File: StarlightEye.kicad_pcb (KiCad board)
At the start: 4 copper layers, 44.3 x 39 mm, 96 parts, among them J1 QWIIC_CONNECTORJS-1MM, J2 FH12A-22S-0.5SH(55), J3 Conn_Coaxial, J4 Conn_Coaxial, J5 Conn_Coaxial, Q1 DMG2302UK-7, Q2 DMG2302UK-7, U1 AP3418KTR-G1, U2 LP5907MFX-1.8, U3 AP2161W, U4 IMX585, U5 ECS-2520MV-240-DN-TR

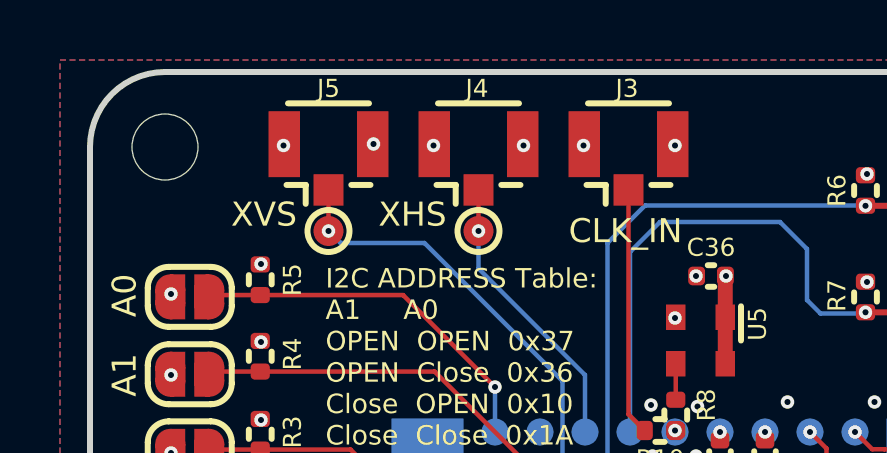
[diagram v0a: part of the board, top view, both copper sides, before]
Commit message: Bug fix: swaping part no AP2161W with AP2171W to have the correct EN polarity
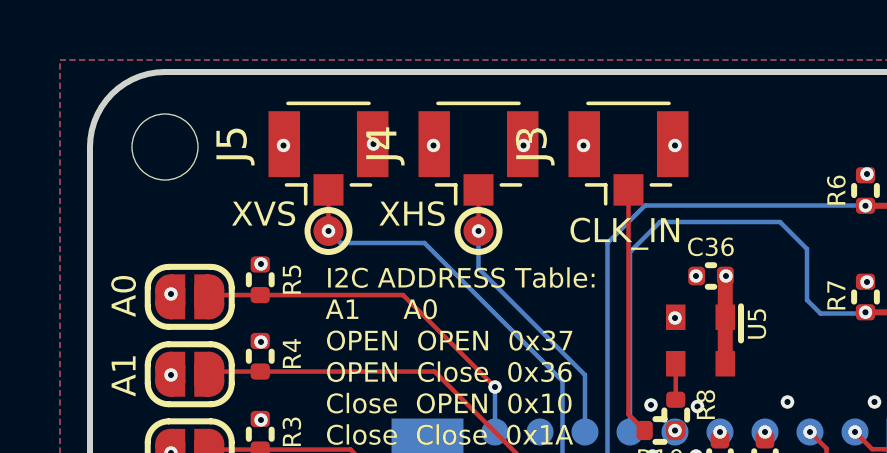
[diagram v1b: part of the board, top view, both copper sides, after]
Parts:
- R1: value 10K -> 13.7K
- R2: value 10K -> 16.5K
- U3: value AP2161W -> AP2171W

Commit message: V1.6 init
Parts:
- removed FB1, FB2: BLM18KG102SN1D, Inductor_SMD:L_0603_1608Metric
- removed Q1, Q2: DMG2302UK-7, Package_TO_SOT_SMD:SOT-23
- removed TP5: TestPoint, TestPoint:TestPoint_Pad_D1.0mm
- added C48: 100nF, Capacitor_SMD:C_0402_1005Metric, F.Cu at (141.1, 110.5)
- added C49: 10nF, Capacitor_SMD:C_0402_1005Metric, F.Cu at (129.4, 111.0)
- added C50: 10uF, Capacitor_SMD:C_0603_1608Metric, F.Cu at (132.7, 107.5)
- added C51: 100nF, Capacitor_SMD:C_0402_1005Metric, F.Cu at (156.6, 120.9)
- added C52: 100nF, Capacitor_SMD:C_0402_1005Metric, F.Cu at (156.6, 119.0)
- added C53: 100nF, Capacitor_SMD:C_0402_1005Metric, F.Cu at (151.6, 117.4)
- added C54: 100nF, Capacitor_SMD:C_0402_1005Metric, F.Cu at (151.7, 120.8)
- added C55: 100nF, Capacitor_SMD:C_0402_1005Metric, F.Cu at (153.4, 89.0)
- added C56: 100nF, Capacitor_SMD:C_0402_1005Metric, F.Cu at (154.2, 94.8)
- added C57: 10nF, Capacitor_SMD:C_0402_1005Metric, F.Cu at (132.3, 105.0)
- added C58: 100pF, Capacitor_SMD:C_0402_1005Metric, F.Cu at (139.2, 117.0)
- added C59: 4.7uF, Capacitor_SMD:C_0603_1608Metric, F.Cu at (126.1, 117.4)
- added C60: C_Feedthrough, footprints:NFM18CC101R1C3D, F.Cu at (155.9, 115.1)
- added C61: 120pF, Capacitor_SMD:C_0402_1005Metric, F.Cu at (129.4, 113.0)
- added C62: 22uF, Capacitor_SMD:C_0805_2012Metric, F.Cu at (128.4, 114.9)
- added D1: MBR0540, Diode_SMD:D_SOD-123, F.Cu at (159.7, 113.9)
- added FB4: BLM18KG102SN1D, Inductor_SMD:L_0402_1005Metric, F.Cu at (141.1, 113.5)
- added J6: Conn_01x02_Shielded, Connector_Molex:Molex_PicoBlade_53398-0271_1x02-1MP_P1.25mm_Vertical, B.Cu at (164.9, 117.3)
- added J7: Conn_01x02_Shielded, Connector_Molex:Molex_PicoBlade_53261-0271_1x02-1MP_P1.25mm_Horizontal, F.Cu at (164.4, 117.7)
- added R11: 10K, Resistor_SMD:R_0402_1005Metric, F.Cu at (155.4, 122.3)
- added R12: 1.15K, Resistor_SMD:R_0402_1005Metric, F.Cu at (130.3, 105.0)
- added R13: 10K, Resistor_SMD:R_0402_1005Metric, F.Cu at (128.4, 113.0)
- added R14: 2K, Resistor_SMD:R_0402_1005Metric, F.Cu at (127.4, 113.0)
- added TP14: TestPoint, TestPoint:TestPoint_Pad_D1.0mm, F.Cu at (131.2, 121.8)
- added TP7: TestPoint, TestPoint:TestPoint_Pad_D1.0mm, F.Cu at (141.4, 121.3)
- added TP_3V1: TestPoint, TestPoint:TestPoint_Pad_D1.0mm, F.Cu at (125.9, 112.8)
- added U10: TVS0500DRV, Package_SON:WSON-6-1EP_2x2mm_P0.65mm_EP1x1.6mm, F.Cu at (158.6, 116.5)
- added U11: TPSM82821SILR, footprints:TPSM82821SILR, F.Cu at (128.4, 117.4)
- added U6: TMP117AIDRVR, footprints:TMP117AIDRVR, F.Cu at (142.9, 110.8)
- added U7: STM8S003F3P, Package_SO:TSSOP-20_4.4x6.5mm_P0.65mm, F.Cu at (146.6, 119.7)
- added U8: DRV8837C, Package_SON:WSON-8-1EP_2x2mm_P0.5mm_EP0.9x1.6mm, F.Cu at (154.7, 119.7)
- added U9: TCA9406DC, footprints:TCA9406DCUR, F.Cu at (153.4, 92.0)
- C13: value 4.7uF -> C_Feedthrough; footprint Capacitor_SMD:C_0603_1608Metric -> footprints:NFM18CC101R1C3D
- C32: value 4.7uF -> 10uF
- J1: value QWIIC_CONNECTORJS-1MM -> Conn_01x04_Shielded
- R6: value 1K -> 10K
- R7: value 1K -> 3.57K
- U3: value AP2171W -> TPS7A90; footprint Package_TO_SOT_SMD:SOT-23-5 -> Package_DFN_QFN:Texas_S-PDSO-N10_EP1.2x2mm
- moved R7 56.5 mm to (131.3, 105.0), turned to 90 degrees
- moved R6 51.2 mm to (147.7, 113.4)
- moved TP1 39.7 mm to (139.1, 113.5)
- moved C22 38.2 mm to (136.1, 115.0)
- moved C24 38.2 mm to (136.1, 120.8)
- moved L1 38.2 mm to (133.6, 116.1)
- moved U1 38.2 mm to (136.3, 118.0)
- moved R1 38.1 mm to (139.2, 118.0)
- moved R2 38.1 mm to (139.2, 119.1)
- moved C32 36.4 mm to (132.0, 111.0), turned to 0 degrees
- moved FB3 36.3 mm to (136.2, 122.5), turned to 0 degrees
- moved C13 35.3 mm to (131.1, 113.1), turned to 90 degrees
- moved U3 34.8 mm to (130.3, 108.1)
- moved C41 34.6 mm to (135.1, 109.4)
- moved TP10 34.5 mm to (137.3, 98.7)
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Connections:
- C13 pad 1: GND -> Net-(C12-Pad2)
- C13 pad 2: Net-(C13-Pad2) -> GND
- C32 pad 1: +3.3VA -> Net-(U3-Pad10)
- FB3 pad 2: +3V3 -> +5V
- J1 pad MP: (no net) -> GND
- J2 pad MP: (no net) -> GND
- JP1 pad 1: GND -> +1V8
- JP2 pad 1: GND -> +1V8
- R4 pad 2: +1V8 -> GND
- R5 pad 1: +1V8 -> ADDR0
- R5 pad 2: ADDR0 -> GND
- R6 pad 1: SCL_1V8 -> CAM_EN
- R6 pad 2: +1V8 -> GND
- R7 pad 1: +1V8 -> Net-(U3-Pad3)
- R7 pad 2: SDA_1V8 -> +3.3VA
- U3 pad 2: GND -> +3.3VA
- U3 pad 3: unconnected-(U3-Pad3) -> Net-(U3-Pad3)
- U3 pad 4: CAM_EN -> GND
- U3 pad 5: Net-(C13-Pad2) -> unconnected-(U3-Pad5)
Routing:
- net +3V3: track 70.9 -> 13.6 mm, vias 2 -> 11
- net SDA_3V3: track 37.7 -> 63.2 mm, vias 2 -> 0
- net SCL_3V3: track 39.3 -> 62.6 mm, vias 0 -> 4
- net +1V8: track 28.2 -> 41.4 mm, vias 21 -> 14
- net Net-(J6-Pad1): track 0.00 -> 10.7 mm, vias 0 -> 1
- net Net-(J6-Pad2): track 0.00 -> 9.68 mm, vias 0 -> 1
- net SLEEP: track 0.00 -> 7.30 mm
- net Net-(J3-Pad1): track 8.24 -> 1.31 mm
- net IN1: track 0.00 -> 6.00 mm
- net Net-(D1-Pad2): track 0.00 -> 6.00 mm
- net CLOCK: track 0.00 -> 5.55 mm
- net Net-(C61-Pad2): track 0.00 -> 5.35 mm
- net IN2: track 0.00 -> 5.05 mm
- net +1V1: track 19.8 -> 15.5 mm, vias 18 -> 19
- net CAM_EN: track 51.0 -> 47.0 mm
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- added copper zone on In2.Cu, net +3V3
- added copper zone on B.Cu, net +5V
- added copper zone on F.Cu, net +5V
- added copper zone on In2.Cu, net +5V
- added copper zone on F.Cu, net Net-(C12-Pad2)
- added copper zone on In2.Cu, net Net-(C12-Pad2)
- added copper zone on F.Cu, net Net-(C60-Pad1)
- added copper zone on F.Cu, net Net-(U3-Pad10)
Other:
- outline, holes or cut-outs redrawn
- board text added: "*"
- board text added: "+"
- board text added: "-"
- board text added: "3V3 FPC"
- board text added: "5V"
- board text added: "5V IN"
- board text added: "AD0"
- board text added: "AD1"
- board text added: "CLK"
- board text added: "Close: MASTER"
- board text added: "FPC Contact Pin Facing UP"
- board text added: "I2C ADDRESS Table: AD1 AD0 OPEN OPEN 0x1A <-Default OPEN Close 0x10 Close OPEN 0x36 Close Close 0x37"
- board text added: "IR Switch"
- board text added: "SWIO"
- board text added: "StarlightEye v1.6 Designed by Will Whang 2024/02/03"
- board text added: "Use FPC with contact pin on the same side"
- board text added: "VINT"
- board text removed: "3V3"
- board text removed: "A0"
- board text removed: "A1"
- board text removed: "CLK_IN"
- board text removed: "Close:MASTER"
- board text removed: "FPC Contact Facing UP"
- board text removed: "I2C ADDRESS Table: A1 A0 OPEN OPEN 0x37 OPEN Close 0x36 Close OPEN 0x10 Close Close 0x1A"
- board text removed: "StarlightEye v1.0 Designed by Will Whang 2023/04/07"

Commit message: V1.7
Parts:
- added C63: 100n, Capacitor_SMD:C_0402_1005Metric, F.Cu at (153.3, 92.6)
- added C64: 10nF, Capacitor_SMD:C_0402_1005Metric, F.Cu at (151.4, 92.6)
- added C65: 2.2uF, Capacitor_SMD:C_0402_1005Metric, F.Cu at (153.3, 93.6)
- added U12: ICM-42688-P, footprints:PQFN50P300X250X97-14N, F.Cu at (152.6, 90.5)
- moved TP4 26.2 mm to (152.6, 115.2)
- moved TP6 3.60 mm to (149.1, 87.0)
- moved U9 3.20 mm to (156.7, 92.0)
- moved C55 3.20 mm to (156.6, 89.0)
- moved C56 3.20 mm to (157.4, 94.8)
- moved C36 1.48 mm to (146.9, 90.2)
- moved U5 1.34 mm to (146.5, 92.2)
- moved R10 1.25 mm to (143.6, 92.5)
- moved R8 1.25 mm to (144.1, 93.0)
- moved TP13 0.35 mm to (130.8, 100.0)
- moved U6 0.25 mm to (142.9, 111.0)
- moved C41 0.20 mm to (135.3, 109.4)
- turned R3 to -90 degrees
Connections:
- JP3 pad 1: GND -> +1V8
- R3 pad 1: XMASTER -> GND
- R3 pad 2: +1V8 -> XMASTER
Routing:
- net XVS: track 14.5 -> 34.2 mm, vias 1 -> 4
- net SCL_1V8: track 15.9 -> 26.5 mm
- net SDA_1V8: track 14.6 -> 25.0 mm
- net +1V8: track 41.4 -> 49.0 mm, vias 14 -> 18
- net GND: track 0.00 -> 6.48 mm, vias 232 -> 253
- net SCL_3V3: track 62.6 -> 59.1 mm
- net SDA_3V3: track 63.2 -> 60.0 mm
- net Net-(J3-Pad1): track 1.31 -> 2.56 mm
- net CLOCK: track 5.55 -> 4.35 mm
- net +3.3VA: track 9.15 -> 8.43 mm
- net Net-(R8-Pad2): track 1.60 -> 1.08 mm
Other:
- board text added: "0x34"
- board text added: "0x48"
- board text added: "0x68"
- board text added: "FPC Contact Facing UP"
- board text added: "JP3"
- board text added: "StarlightEye v1.7 Designed by Will Whang 2024/08/03"
- board text added: "X"
- board text added: "Y"
- board text added: "Z"
- board text removed: "Close: MASTER"
- board text removed: "FPC Contact Pin Facing UP"
- board text removed: "StarlightEye v1.6 Designed by Will Whang 2024/02/03"

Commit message: Ver 2.0 HW
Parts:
- removed D1: MBR0540, Diode_SMD:D_SOD-123
- removed J7: Conn_01x02_Shielded, Connector_Molex:Molex_PicoBlade_53261-0271_1x02-1MP_P1.25mm_Horizontal
- removed TP11, TP12, TP14, TP6: TestPoint, TestPoint:TestPoint_Pad_D1.0mm
- removed U12: ICM-42688-P, footprints:PQFN50P300X250X97-14N
- added C66: 10nF, Capacitor_SMD:C_0402_1005Metric, F.Cu at (111.4, 56.9)
- added C67: 1uF, Capacitor_SMD:C_0402_1005Metric, F.Cu at (113.3, 57.9)
- added R21: DNP, Resistor_SMD:R_0402_1005Metric, F.Cu at (106.7, 53.2)
- added R22: DNP, Resistor_SMD:R_0402_1005Metric, F.Cu at (108.1, 53.2)
- added TP5: TestPoint, TestPoint:TestPoint_Pad_D1.0mm, F.Cu at (99.7, 53.4)
- C13: value C_Feedthrough -> NFM18PC104R1C3D
- C48: value 100nF -> 1uF
- C49: value 10nF -> 1uF
- C50: value 10uF -> 22uF
- C59: value 4.7uF -> 22uF
- C60: value C_Feedthrough -> 47uF; footprint footprints:NFM18CC101R1C3D -> Capacitor_SMD:C_0603_1608Metric
- C61: value 120pF -> 100pF
- C62: value 22uF -> 47uF; footprint Capacitor_SMD:C_0805_2012Metric -> Capacitor_SMD:C_0603_1608Metric
- C63: value 100n -> 22uF; footprint Capacitor_SMD:C_0402_1005Metric -> Capacitor_SMD:C_0603_1608Metric
- C64: value 10nF -> 10uF; footprint Capacitor_SMD:C_0402_1005Metric -> Capacitor_SMD:C_0603_1608Metric
- C65: value 2.2uF -> 100nF
- FL1, FL2, FL3, FL4, FL5: value DLP11SN900HL2L -> DLM0QSB120HY2D; footprint footprints:DLP11SA350HL2B -> footprints:DLM0QSB120HY2D
- J1: footprint Connector_JST:JST_SH_SM04B-SRSS-TB_1x04-1MP_P1.00mm_Horizontal -> Connector_JST:JST_SH_BM04B-SRSS-TB_1x04-1MP_P1.00mm_Vertical
- J2: value FH12A-22S-0.5SH(55) -> TF38-22S-0.5SV(830); footprint Connector_FFC-FPC:Hirose_FH12-22S-0.5SH_1x22-1MP_P0.50mm_Horizontal -> footprints:TF3822S05SV830
- J6: footprint Connector_Molex:Molex_PicoBlade_53398-0271_1x02-1MP_P1.25mm_Vertical -> Connector_Molex:Molex_PicoBlade_53261-0271_1x02-1MP_P1.25mm_Horizontal; moved to F.Cu
- R10: value 22R -> DNP
- R13: value 10K -> 562K
- R14: value 2K -> 91K
- U10: value TVS0500DRV -> TPSM83100SIUR; footprint Package_SON:WSON-6-1EP_2x2mm_P0.65mm_EP1x1.6mm -> footprints:MICROSIP8_SIU_TEX-L
- U11: value TPSM82821SILR -> ICM-42688-P; footprint footprints:TPSM82821SILR -> footprints:PQFN50P300X250X97-14N
- U5: value ECS-2520MV-240-DN-TR -> SX2M24.000M20F30TNN
- U7: value STM8S003F3P -> CH32V003F4P6
- moved U10 77.4 mm to (88.4, 83.8), turned to -90 degrees
- moved C60 77.4 mm to (86.8, 80.2), turned to 0 degrees
- moved TP9 65.0 mm to (90.1, 87.1)
- moved C63 64.6 mm to (89.9, 80.2), turned to 0 degrees
- moved U11 64.5 mm to (112.4, 54.9), turned to 0 degrees
- moved R6 64.1 mm to (90.5, 84.5)
- moved R11 62.7 mm to (108.1, 81.3)
- moved C51 61.0 mm to (110.8, 80.5), turned to -90 degrees
- moved C54 61.0 mm to (105.1, 81.3), turned to 180 degrees
- moved J6 60.8 mm to (112.7, 86.1), turned to 0 degrees
- moved C53 60.5 mm to (103.1, 81.3)
- moved C52 59.2 mm to (110.3, 82.0), turned to 0 degrees
- moved U8 57.1 mm to (112.7, 81.0), turned to 90 degrees
- moved FB3 55.0 mm to (93.8, 87.4)
- moved C56 54.6 mm to (116.4, 58.8)
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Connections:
- net Net-(FL1-Pad2) renamed /D0_N
- net Net-(FL1-Pad3) renamed /D0_P
- net Net-(FL2-Pad2) renamed /D1_N
- net Net-(FL2-Pad3) renamed /D1_P
- net Net-(FL3-Pad2) renamed /CLK_N
- net Net-(FL3-Pad3) renamed /CLK_P
- net Net-(FL4-Pad2) renamed /D2_N
- net Net-(FL4-Pad3) renamed /D2_P
- net Net-(FL5-Pad2) renamed /D3_N
- net Net-(FL5-Pad3) renamed /D3_P
- C12 pad 2: Net-(C12-Pad2) -> +3.6V
- C13 pad 1: Net-(C12-Pad2) -> +3.6V
- C24 pad 1: Net-(C24-Pad1) -> Net-(U1-VIN)
- C52 pad 2: +5V -> +3.6V
- C59 pad 2: +5V -> +3V3
- C60 pad 1: Net-(C60-Pad1) -> +3.6V
- C61 pad 1: Net-(C12-Pad2) -> +3.6V
- C61 pad 2: Net-(C61-Pad2) -> Net-(U10-FB)
- C62 pad 1: Net-(C12-Pad2) -> +3.6V
- C63 pad 1: +1V8 -> GND
- C63 pad 2: GND -> +3V3
- C64 pad 1: +1V8 -> GND
- C64 pad 2: GND -> +3.6V
- FB3 pad 1: Net-(C24-Pad1) -> +3V3
- FB3 pad 2: +5V -> Net-(U1-VIN)
- J3 pad 1: Net-(J3-Pad1) -> Net-(J3-In)
- R10 pad 1: CLOCK -> Net-(J3-In)
- R10 pad 2: Net-(J3-Pad1) -> CLOCK
- R13 pad 1: Net-(C61-Pad2) -> Net-(U10-FB)
- R13 pad 2: Net-(C12-Pad2) -> +3.6V
- R14 pad 2: Net-(C61-Pad2) -> Net-(U10-FB)
- TP_3V1 pad 1: Net-(C12-Pad2) -> +3.6V
- U1 pad 4: Net-(C24-Pad1) -> Net-(U1-VIN)
- U10 pad 1: GND -> +3V3
- U10 pad 4: Net-(C60-Pad1) -> +3.6V
- U10 pad 5: Net-(C60-Pad1) -> Net-(U10-FB)
- U10 pad 6: Net-(C60-Pad1) -> GND
- U10 pad 7: GND -> +3V3
- U11 pad 1: +5V -> GND
- U11 pad 2: +5V -> GND
- U11 pad 3: +5V -> GND
- U11 pad 5: Net-(C12-Pad2) -> +1V8
- U11 pad 6: Net-(C12-Pad2) -> GND
- U11 pad 7: Net-(C12-Pad2) -> GND
- U11 pad 8: Net-(C61-Pad2) -> +1V8
- U11 pad 9: GND -> XVS
- U2 pad 1: Net-(C12-Pad2) -> +3.6V
- U8 pad 1: +5V -> +3.6V
- U9 pad 1: SDA_3V3 -> SCL_3V3
- U9 pad 4: SDA_1V8 -> SCL_1V8
- U9 pad 5: SCL_1V8 -> SDA_1V8
- U9 pad 8: SCL_3V3 -> SDA_3V3
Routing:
- net +3.6V: track 0.00 -> 37.1 mm, vias 0 -> 2
- net +1V8: track 49.0 -> 16.0 mm, vias 18 -> 17
- net CAM_EN: track 47.0 -> 64.3 mm, vias 3 -> 6
- net +3V3: track 13.5 -> 4.57 mm, vias 11 -> 22
- net Net-(J3-In): track 0.00 -> 8.64 mm
- net Net-(J6-Pin_1): track 10.7 -> 2.11 mm, vias 1 -> 2
- net Net-(J6-Pin_2): track 9.68 -> 2.11 mm, vias 1 -> 0
- net IN2: track 5.05 -> 11.2 mm
- net Net-(D1-Pad2): track 6.08 -> 0.00 mm
- net Net-(C61-Pad2): track 5.35 -> 0.00 mm
- net CLOCK: track 4.35 -> 0.04 mm
- net IN1: track 6.00 -> 9.64 mm
- net Net-(C24-Pad1): track 3.45 -> 0.00 mm
- net Net-(U1-VIN): track 0.00 -> 3.31 mm
- net Net-(U10-FB): track 0.00 -> 3.21 mm
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- added copper zone on B.Cu, net +3.6V
- added copper zone on F.Cu, net +3.6V
- added copper zone on B.Cu, net +3V3
- removed copper zone on B.Cu, net +5V
- removed copper zone on F.Cu, net +5V
- removed copper zone on In2.Cu, net +5V
- removed copper zone on F.Cu, net Net-(C12-Pad2)
- removed copper zone on In2.Cu, net Net-(C12-Pad2)
- removed copper zone on F.Cu, net Net-(C60-Pad1)
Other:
- board size 44.3 x 39 mm -> 39 x 39 mm
- board text added: "3V3"
- board text added: "3V6"
- board text added: "Cam View"
- board text added: "Close: Follower"
- board text added: "Color"
- board text added: "FPC Contact Facing Inward"
- board text added: "I2C ADDRESS Table: AD1 AD0 OPEN OPEN 0x1A OPEN Close 0x10 Close OPEN 0x36 Close Close 0x37"
- board text added: "IR"
- board text added: "LATCH ->"
- board text added: "Mono"
- board text added: "StarlightEye V2 Designed by W.W"
- board text added: "Use FPC with contact on the same side!"
- board text removed: "+"
- board text removed: "-"
- board text removed: "3V3 FPC"
- board text removed: "5V"
- board text removed: "5V IN"
- board text removed: "FPC Contact Facing UP"
- board text removed: "I2C ADDRESS Table: AD1 AD0 OPEN OPEN 0x1A <-Default OPEN Close 0x10 Close OPEN 0x36 Close Close 0x37"
- board text removed: "IR Switch"
- board text removed: "JP3"
- board text removed: "StarlightEye v1.7 Designed by Will Whang 2024/08/03"
- board text removed: "Use FPC with contact pin on the same side"
- board text removed: "VINT"
